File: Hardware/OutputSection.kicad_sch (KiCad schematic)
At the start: 20 parts, among them Q1 MMBT3904, Q2 MMBT3904, Q3 MMBT3904, Q4 MMBT3904, Q5 MMBT3904

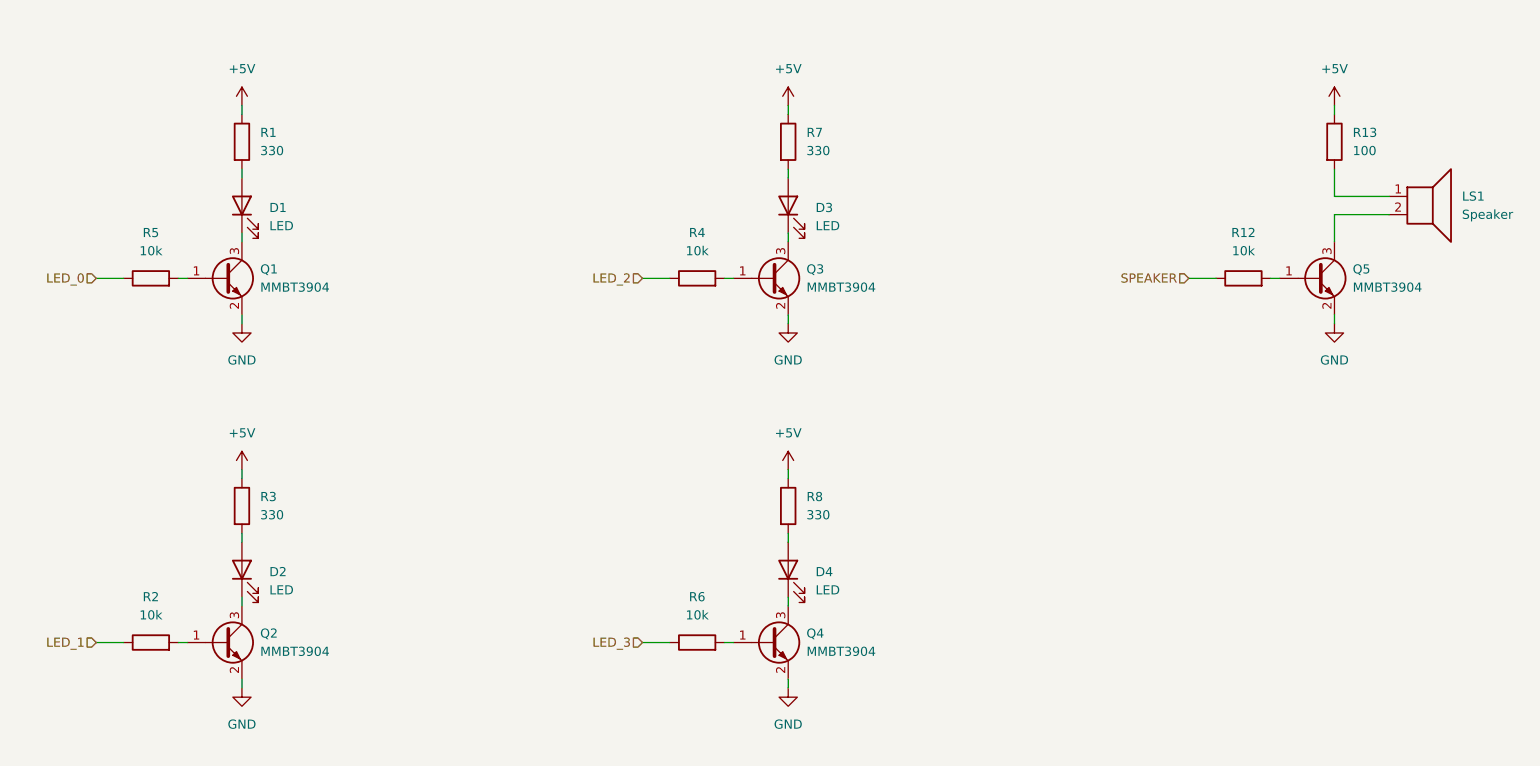
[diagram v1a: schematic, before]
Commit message: Updated KiCAD project.
- Added grouping in schematics.
- Removed unnecessary net names in "LogicSection.kicad_sch".
- Added 330R between +5V and nREG_ENABLE.
- Changed path for 3D models.
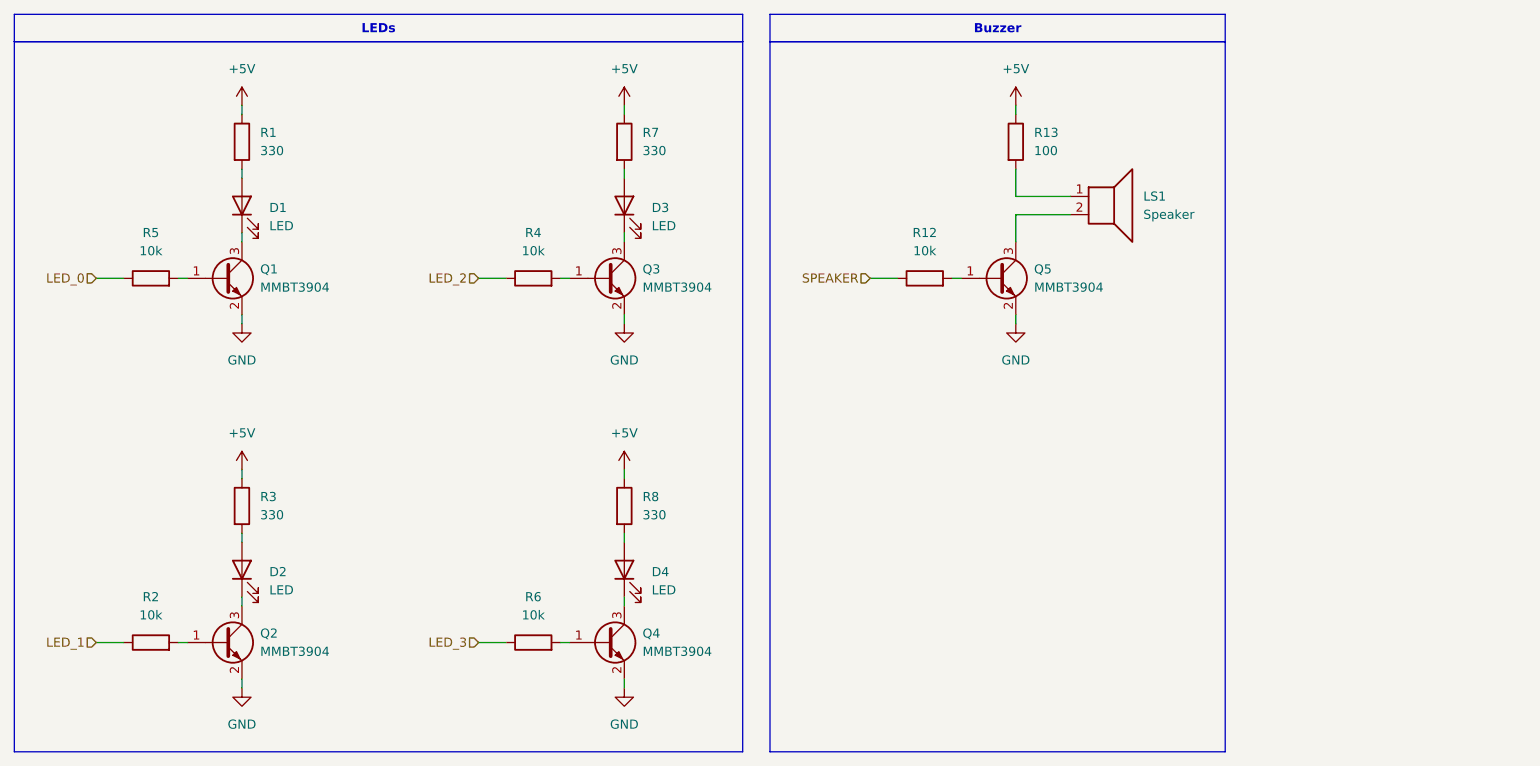
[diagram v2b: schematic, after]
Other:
- moved on the sheet: D3, D4, LS1, Q3, Q4, Q5, R12, R13, R4, R6, R7, R8
